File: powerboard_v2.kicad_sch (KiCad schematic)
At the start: 16 parts, among them J1 Conn_01x02_Pin, J4 Conn_01x02_Pin, J5 Conn_01x02_Pin, K3 Relay_SPDT, K4 Relay_SPDT, U5 TLP785

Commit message: ver1かんせい
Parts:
- R2: footprint Resistor_THT:R_Axial_DIN0516_L15.5mm_D5.0mm_P7.62mm_Vertical -> Resistor_THT:R_Axial_DIN0516_L15.5mm_D5.0mm_P5.08mm_Vertical
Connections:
- net +24V: now also D1.1 (K), D3.1 (K), K3.A2, K4.A2; no longer D1.2 (A), D3.2 (A), K3.A1, K4.A1
- net photo in: now also D1.2 (A), D3.2 (A), K3.A1, K4.A1; no longer D1.1 (K), D3.1 (K), K3.A2, K4.A2
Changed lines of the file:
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@@
 	(paper "A4")
+	(junction
+		(at 144.78 52.07)
+		(diameter 0)
+		(color 0 0 0 0)
+	)
 	(junction
 		(at 140.97 69.85)
@@
 	)
 	(junction
-		(at 144.78 52.07)
-		(diameter 0)
-		(color 0 0 0 0)
-	)
-	(junction
 		(at 46.99 48.26)
 		(diameter 0)
@@
 	)
 	(junction
+		(at 137.16 52.07)
+		(diameter 0)
+		(color 0 0 0 0)
+	)
+	(junction
 		(at 67.31 77.47)
 		(diameter 0)
@@
 	)
 	(junction
-		(at 137.16 52.07)
-		(diameter 0)
-		(color 0 0 0 0)
-	)
-	(junction
 		(at 140.97 38.1)
-		(diameter 0)
-		(color 0 0 0 0)
-	)
-	(junction
-		(at 140.97 52.07)
 		(diameter 0)
 		(color 0 0 0 0)
@@
 	(wire
 		(pts
+			(xy 137.16 52.07) (xy 144.78 52.07)
+		)
+		(stroke
+			(width 0)
+			(type default)
+		)
+	)
+	(wire
+		(pts
 			(xy 137.16 57.15) (xy 137.16 52.07)
 		)
@@
 	(wire
 		(pts
-			(xy 140.97 38.1) (xy 140.97 52.07)
-		)
-		(stroke
-			(width 0)
-			(type default)
-		)
-	)
-	(wire
-		(pts
 			(xy 44.45 68.58) (xy 45.72 68.58)
 		)
@@
 	(wire
 		(pts
-			(xy 140.97 71.12) (xy 140.97 69.85)
-		)
-		(stroke
-			(width 0)
-			(type default)
-		)
-	)
-	(wire
-		(pts
-			(xy 137.16 52.07) (xy 140.97 52.07)
-		)
-		(stroke
-			(width 0)
-			(type default)
-		)
-	)
-	(wire
-		(pts
 			(xy 55.88 52.07) (xy 58.42 52.07)
 		)
@@
 	(wire
 		(pts
+			(xy 140.97 38.1) (xy 140.97 69.85)
+		)
+		(stroke
+			(width 0)
+			(type default)
+		)
+	)
+	(wire
+		(pts
 			(xy 137.16 64.77) (xy 137.16 69.85)
 		)
@@
 		(pts
 			(xy 55.88 44.45) (xy 58.42 44.45)
-		)
-		(stroke
-			(width 0)
-			(type default)
-		)
-	)
-	(wire
-		(pts
-			(xy 140.97 52.07) (xy 144.78 52.07)
 		)
 		(stroke
@@
 		)
 	)
-	(global_label "photo in"
-		(shape input)
-		(at 140.97 71.12 270)
-		(fields_autoplaced yes)
-		(effects
-			(font
-				(size 1.27 1.27)
-			)
-			(justify right)
-		)
-		(property "Intersheetrefs" "${INTERSHEET_REFS}"
-			(at 140.97 82.1483 90)
-			(effects
-				(font
-					(size 1.27 1.27)
-				)
-				(justify right)
-				(hide yes)
-			)
-		)
-	)
 	(global_label "xt60_out"
 		(shape input)
@@
 				)
 				(justify right)
+				(hide yes)
+			)
+		)
+	)
+	(global_label "photo in"
+		(shape input)
+		(at 134.62 52.07 90)
+		(fields_autoplaced yes)
+		(effects
+			(font
+				(size 1.27 1.27)
+			)
+			(justify left)
+		)
+		(property "Intersheetrefs" "${INTERSHEET_REFS}"
+			(at 134.62 41.0417 90)
+			(effects
+				(font
+					(size 1.27 1.27)
+				)
+				(justify left)
 				(hide yes)
 			)
@@
 			)
 		)
-		(property "Footprint" "Resistor_THT:R_Axial_DIN0516_L15.5mm_D5.0mm_P7.62mm_Vertical"
+		(property "Footprint" "Resistor_THT:R_Axial_DIN0516_L15.5mm_D5.0mm_P5.08mm_Vertical"
 			(at 93.218 77.47 90)
 			(effects

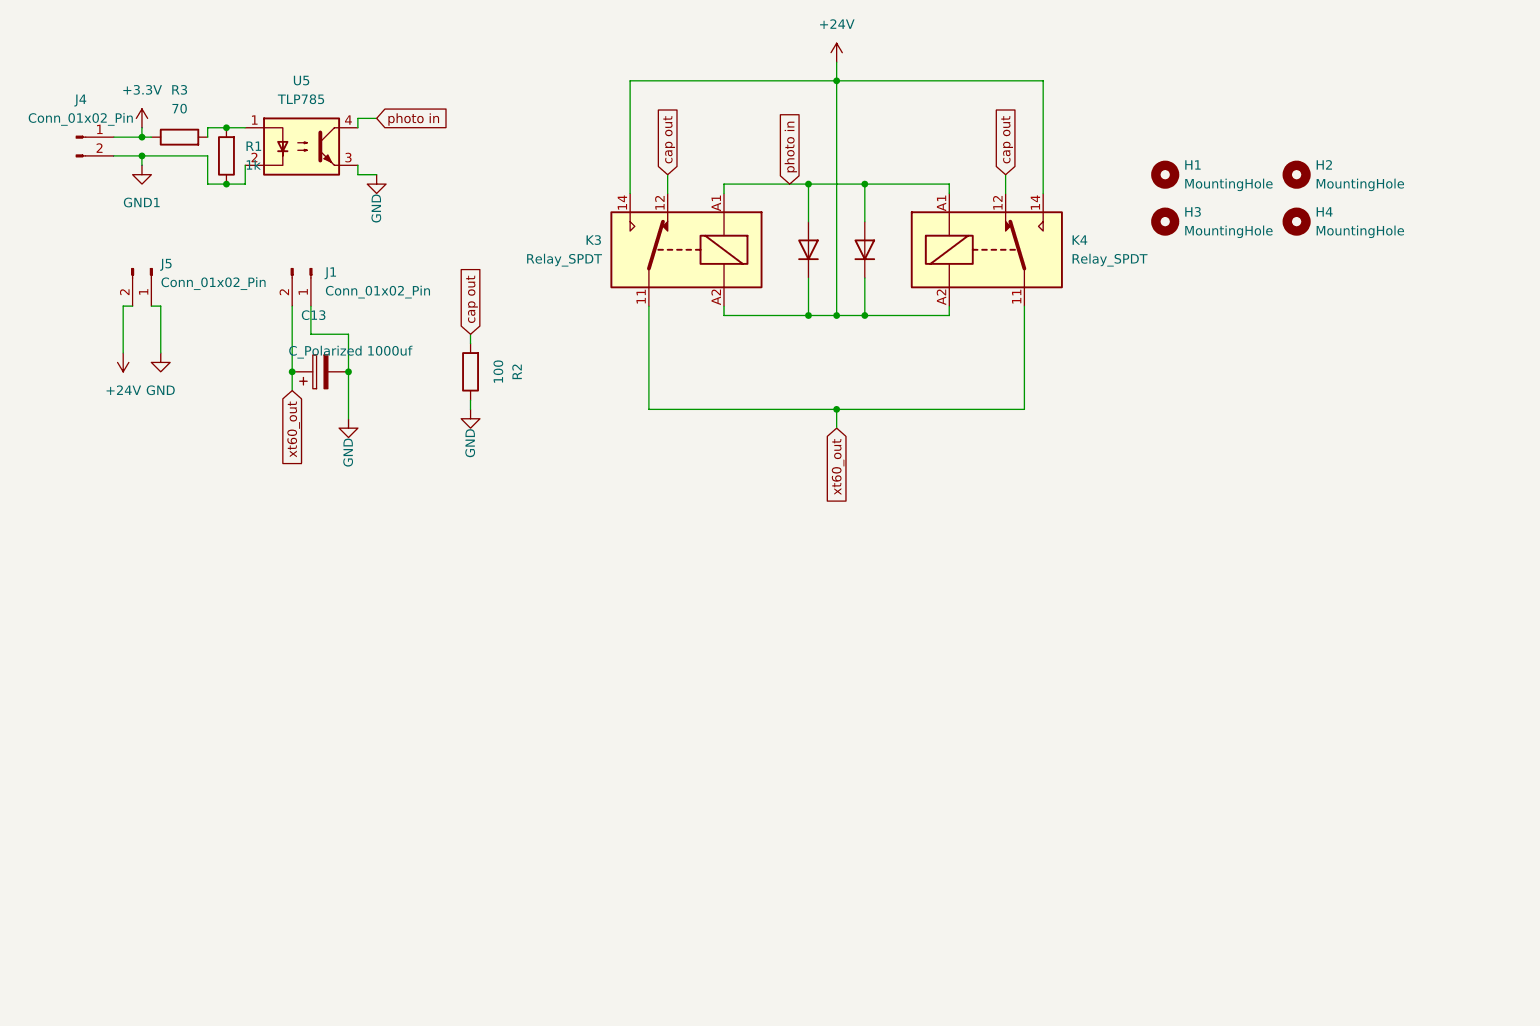
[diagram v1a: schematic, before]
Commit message: 改良版作成開始　dcdcの配置
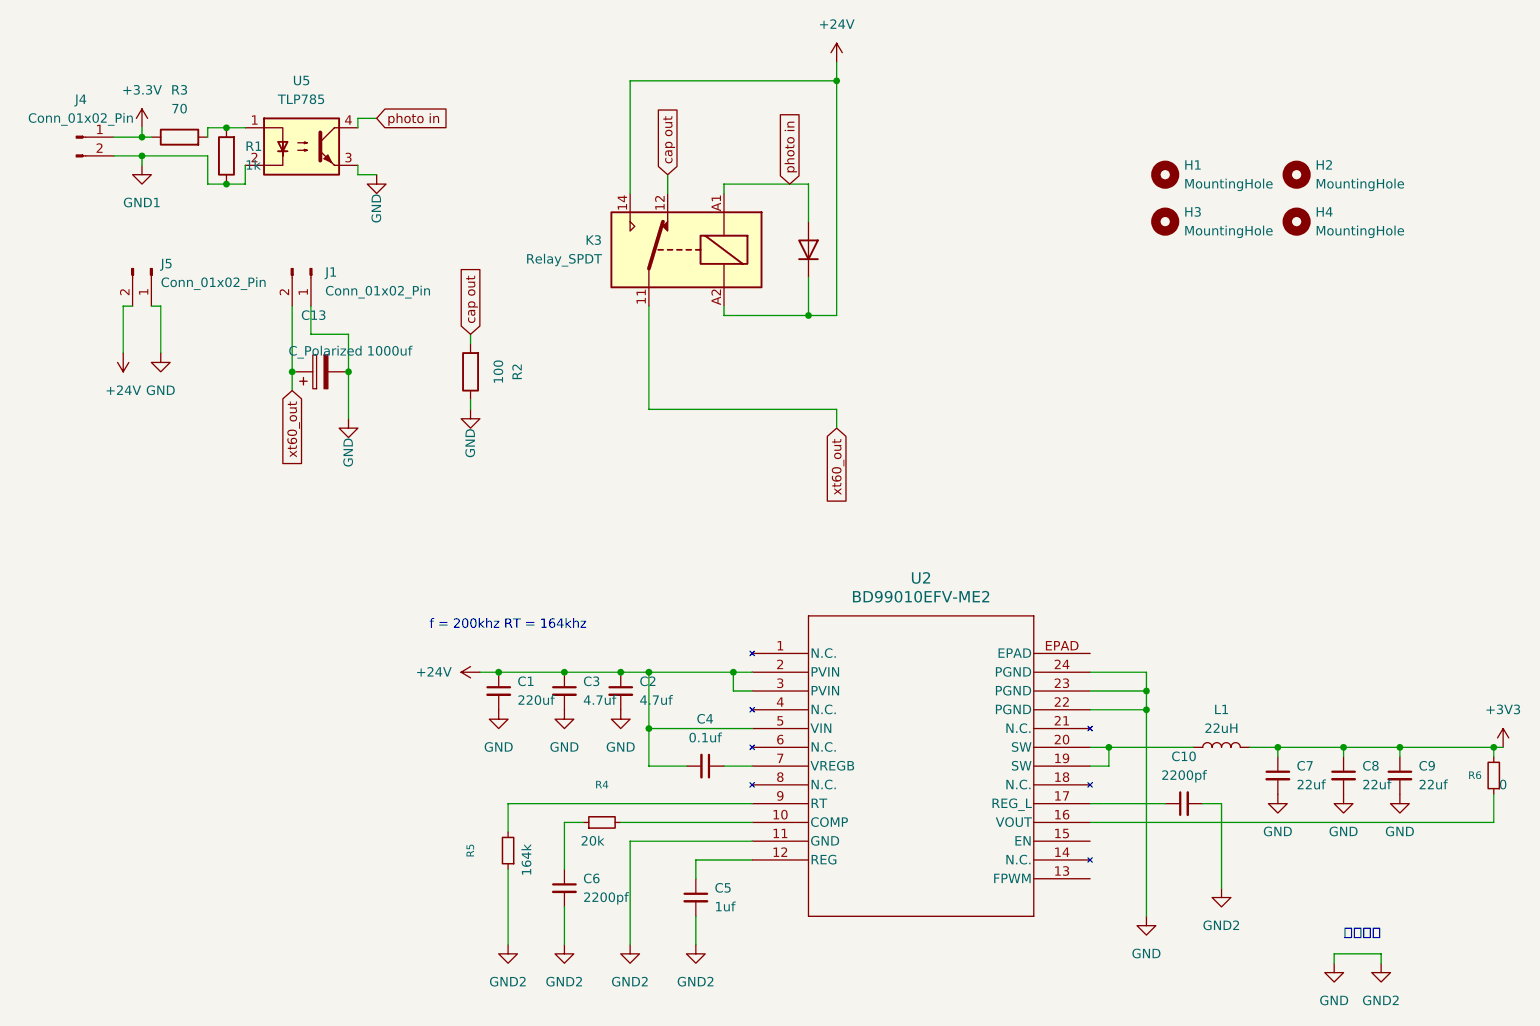
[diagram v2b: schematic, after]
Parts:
- removed D3: D, Diode_SMD:D_SMA, symbol Device:D
- removed K4: Relay_SPDT, Relay_THT:Relay_SPDT_RAYEX-L90S, symbol Relay:Relay_SPDT
- added C1: 220uf, Capacitor_THT:CP_Radial_D10.0mm_P5.00mm, symbol Device:C_Small
- added C10: 2200pf, symbol Device:C_Small
- added C2, C3: 4.7uf, Capacitor_SMD:C_0603_1608Metric_Pad1.08x0.95mm_HandSolder, symbol Device:C_Small
- added C4: 0.1uf, Capacitor_SMD:C_0603_1608Metric_Pad1.08x0.95mm_HandSolder, symbol Device:C_Small
- added C5: 1uf, Capacitor_SMD:C_0603_1608Metric_Pad1.08x0.95mm_HandSolder, symbol Device:C_Small
- added C6: 2200pf, Capacitor_SMD:C_0603_1608Metric_Pad1.08x0.95mm_HandSolder, symbol Device:C_Small
- added C7, C8, C9: 22uf, symbol Device:C_Small
- added L1: 22uH, symbol Device:L
- added R4: 20k, symbol Device:R_Small
- added R5: 164k, symbol Device:R_Small
- added R6: 0, symbol Device:R_Small
- added U2: BD99010EFV-ME2, BD99010:HTSSOP-B24_ROM, symbol BD99010:BD99010EFV-ME2
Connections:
- net +24V: now also C1.1, C2.1, C3.1, C4.2, U2.2 (PVIN), U2.3 (PVIN), U2.5 (VIN)
- net GND: now also C1.2, C10.2, C2.2, C3.2, C5.2, C6.2, C7.2, C8.2, C9.2, R5.1, U2.11 (GND), U2.22 (PGND), U2.23 (PGND), U2.24 (PGND)
- new net: C5.1, U2.12 (REG)
- new net: C4.1, U2.7 (VREGB)
- new net: C6.1, R4.1
- new net: R5.2, U2.9 (RT)
- new net: L1.1, U2.19 (SW), U2.20 (SW)
- new net: R6.1, U2.16 (VOUT)
- new net: C10.1, U2.17 (REG_L)
- new net: R4.2, U2.10 (COMP)
- new net +3V3: C7.1, C8.1, C9.1, L1.2, R6.2
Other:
- note added: "f = 200khz RT = 164khz"
- note added: "他店設置"

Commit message: 降圧回路の搭載
降圧用dcdcなどを置いた　次部品配置
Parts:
- added J2, J3: Conn_01x02_Pin, Connector_AMASS:AMASS_XT30PW-F_1x02_P2.50mm_Horizontal, symbol Connector:Conn_01x02_Pin
- C10: footprint (none) -> Capacitor_SMD:C_0603_1608Metric_Pad1.08x0.95mm_HandSolder
- C7, C8, C9, R4, R5, R6: footprint (none) -> Resistor_SMD:R_0603_1608Metric_Pad0.98x0.95mm_HandSolder
- L1: footprint (none) -> Inductor_THT:L_Radial_D12.0mm_P5.00mm_Neosid_SD12k_style2
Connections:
- net +24V: now also U2.15 (EN); no longer C1.1, C2.1, C3.1, C4.2, U2.2 (PVIN), U2.3 (PVIN), U2.5 (VIN)
- net +3V3: now also J3.2 (Pin_2)
- net GND: no longer C10.2, C5.2, C6.2, C7.2, C8.2, C9.2, R5.1, U2.11 (GND), U2.22 (PGND), U2.23 (PGND), U2.24 (PGND)
- net at R6.1, U2.16 (VOUT): now also U2.13 (FPWM)
- net GND2: now reaches U2.EPAD
- net GND2: now also C10.2, C5.2, C6.2, C7.2, C8.2, C9.2, R5.1, U2.11 (GND), U2.22 (PGND), U2.23 (PGND), U2.24 (PGND), J2.1 (Pin_1), J3.1 (Pin_1)
- new net +7.5V: C1.1, C2.1, C3.1, C4.2, J2.2 (Pin_2), U2.2 (PVIN), U2.3 (PVIN), U2.5 (VIN)
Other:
- note removed: "他店設置"

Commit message: ver2粗方完成(粗はある)
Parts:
- added JP1, JP2: SolderJumper_2_Open, Jumper:SolderJumper-2_P1.3mm_Open_RoundedPad1.0x1.5mm, symbol Jumper:SolderJumper_2_Open
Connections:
- net +24V: no longer U2.15 (EN)
- net +7.5V: now also U2.15 (EN), JP1.2 (B)
- net GND: now also JP2.1 (A); no longer C1.2, C2.2, C3.2
- net GND2: now also C1.2, C2.2, C3.2, JP2.2 (B)
- net xt60_out: now also JP1.1 (A)
